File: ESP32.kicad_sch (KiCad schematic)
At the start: 32 parts, among them IC1 ESDALC6V1W5, J4 USB_B_Micro, Q7 IRLML6402, SW2 SW_DIP_x01, SW3 SW_DIP_x01, U3 ESP32-C6-WROOM-1-N8, U4 AMS1117-3.3

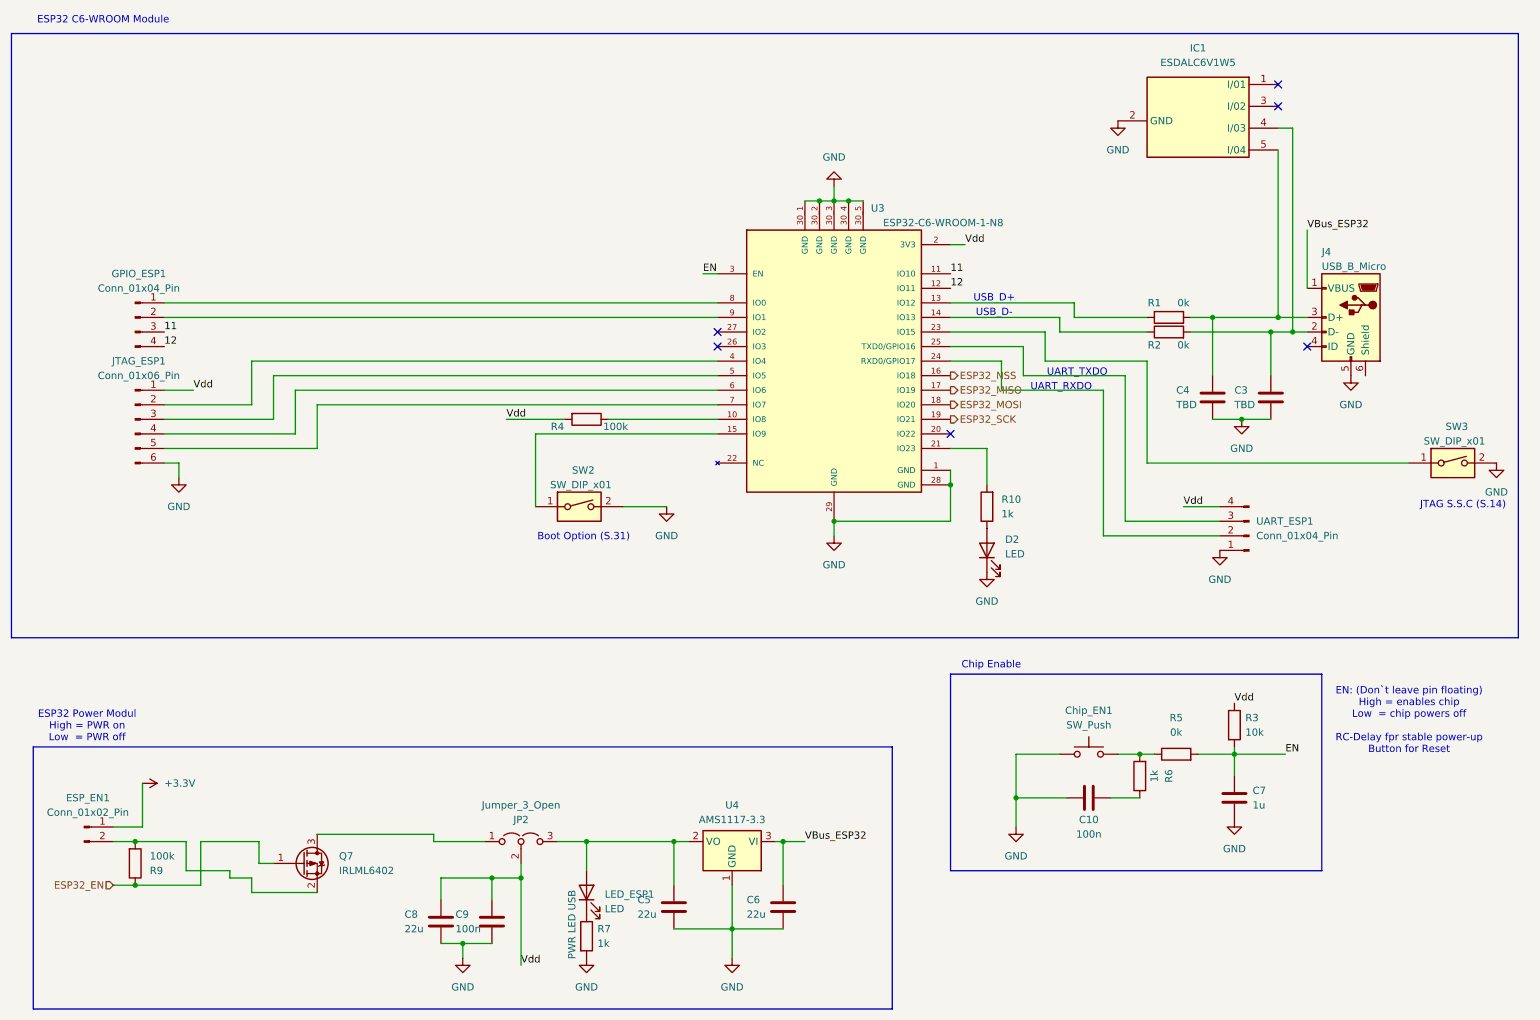
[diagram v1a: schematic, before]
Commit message: new layout
- recreation of the layout
- changed connection of ADC to MCU
- cleaner layout
- battery (supercap) for rtc
- crystal nearby the mcu
- 3V3 layer can be switched on/off separated from the mcu
- diode replaced with MOSFET
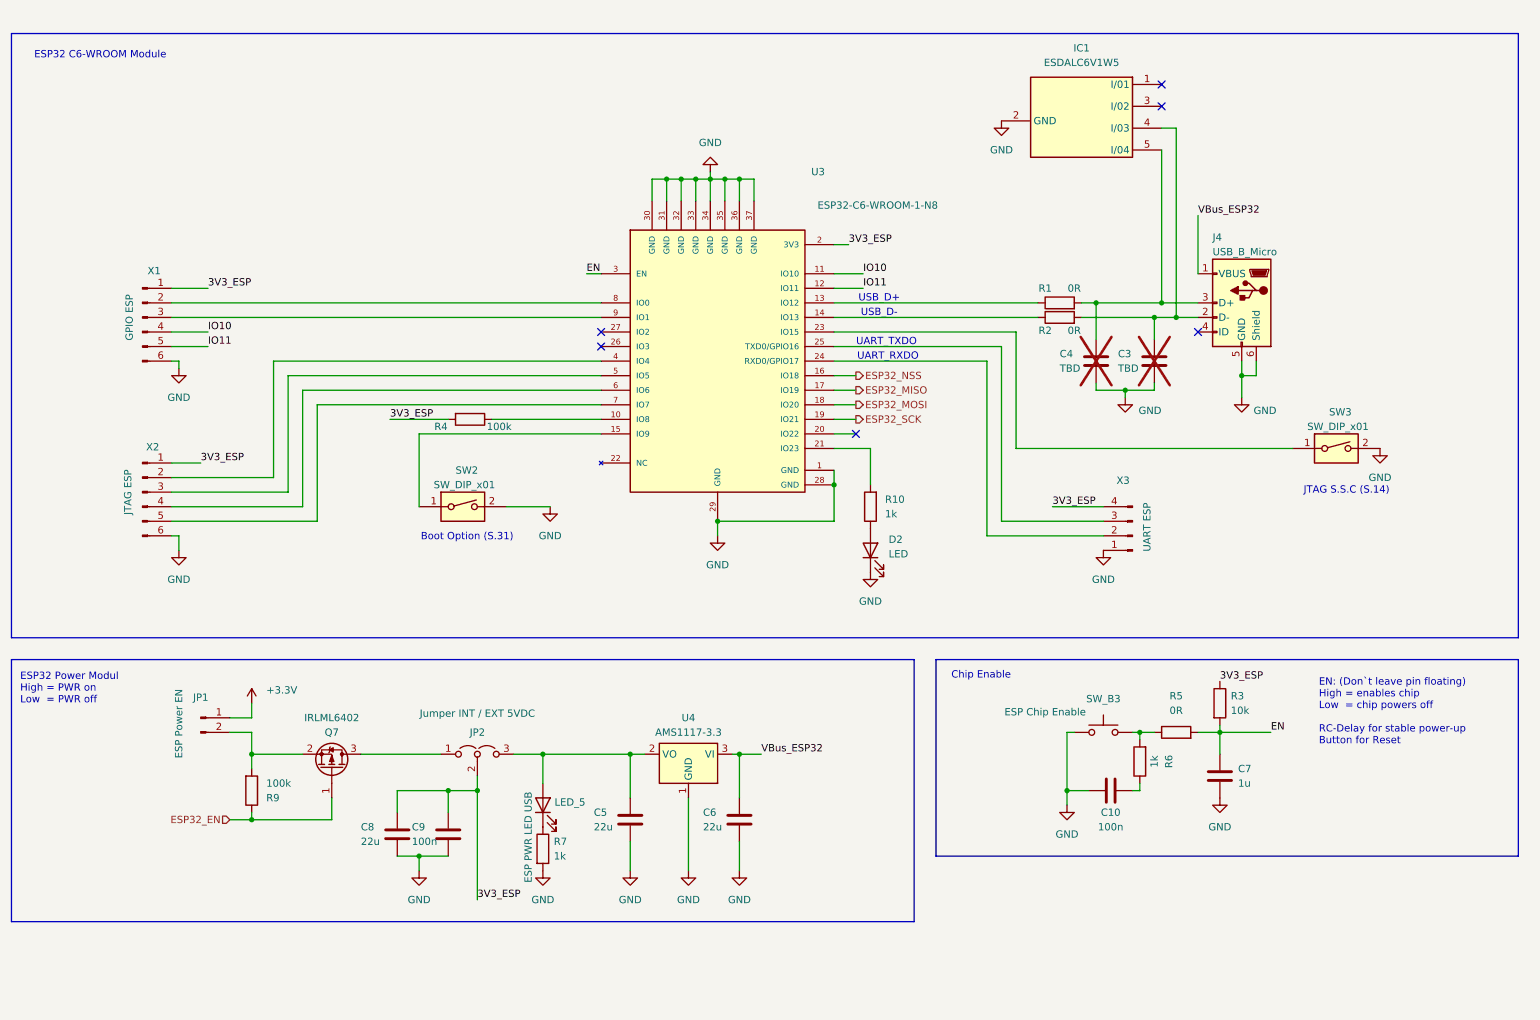
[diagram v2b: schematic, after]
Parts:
- removed GPIO_ESP1: Conn_01x04_Pin, Connector_PinHeader_2.54mm:PinHeader_1x04_P2.54mm_Vertical, symbol Connector:Conn_01x04_Pin
- added X1: Conn_01x06_Pin, Connector_PinHeader_2.54mm:PinHeader_1x06_P2.54mm_Vertical, symbol Connector:Conn_01x06_Pin
- C3, C4: now not fitted
- C9: Mouser Part Number 187-CL21A226KQCLRNC -> 603-CC805KRX7R9BB104
- J4: Mouser Part Number 649-10103594-0001LF -> 649-10103594-0001LF
- JP1: renamed from ESP_EN1; Mouser Part Number (none) -> 523-G800NA306018EU
- JP2: Mouser Part Number (none) -> 649-1012937890304BLF
- Q7: Mouser Part Number (none) -> 942-IRLML6402TRPBF
- R1, R2, R5: value 0k -> 0R
- U3: footprint ESP32-C6-WROOM-1-N8:XCVR_ESP32-C6-WROOM-1-N8 -> Bibliothek:ESP32C6WROOM1N8
- U4: Mouser Part Number 926-LM1117MPX3.3NOPB -> 926-LM1117MP-3.3NOPB
- X2: renamed from JTAG_ESP1; Mouser Part Number (none) -> 649-1012937990602BLF
- X3: renamed from UART_ESP1; Mouser Part Number (none) -> 523-G800LW304032EU
- renumbered LED_ESP1 to LED_5, Chip_EN1 to SW_B3
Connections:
- net GND: now also J4.6 (Shield), U3.30 (GND), U3.31 (GND), U3.32 (GND), U3.33 (GND), U3.34 (GND), U3.35 (GND), U3.36 (GND), U3.37 (GND), X1.6 (Pin_6); no longer U3.30_1 (GND), U3.30_2 (GND), U3.30_3 (GND), U3.30_4 (GND), U3.30_5 (GND)
- net at U3.8 (IO0): now also X1.2 (Pin_2)
- net at U3.9 (IO1): now also X1.3 (Pin_3)
- net 11 renamed IO10
- net IO10: now also X1.4 (Pin_4)
- net 12 renamed IO11
- net IO11: now also X1.5 (Pin_5)
- net Vdd renamed 3V3_ESP
- net 3V3_ESP: now also X1.1 (Pin_1)
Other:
- note added: "EN: (Don`t leave pin floating) High = enables chip Low = chip powers off RC-Delay for stable power-up Button for Reset"
- note removed: "EN: (Don`t leave pin floating) High = enables chip Low = chip powers off RC-Delay fpr stable power-up Button for Reset"
- moved on the sheet: C10, C5, C6, C7, C8, C9, D2, IC1, J4, JP1, JP2, LED_5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
